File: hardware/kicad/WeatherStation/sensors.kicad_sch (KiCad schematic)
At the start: 16 parts, among them J4 Anemometer (RJ11), J5 Rain Gauge (RJ11), U4 BME280 (0x76), U5 AS5600 (0x36), U6 SI1145 (0x60), U7 BH1750 (0x23)

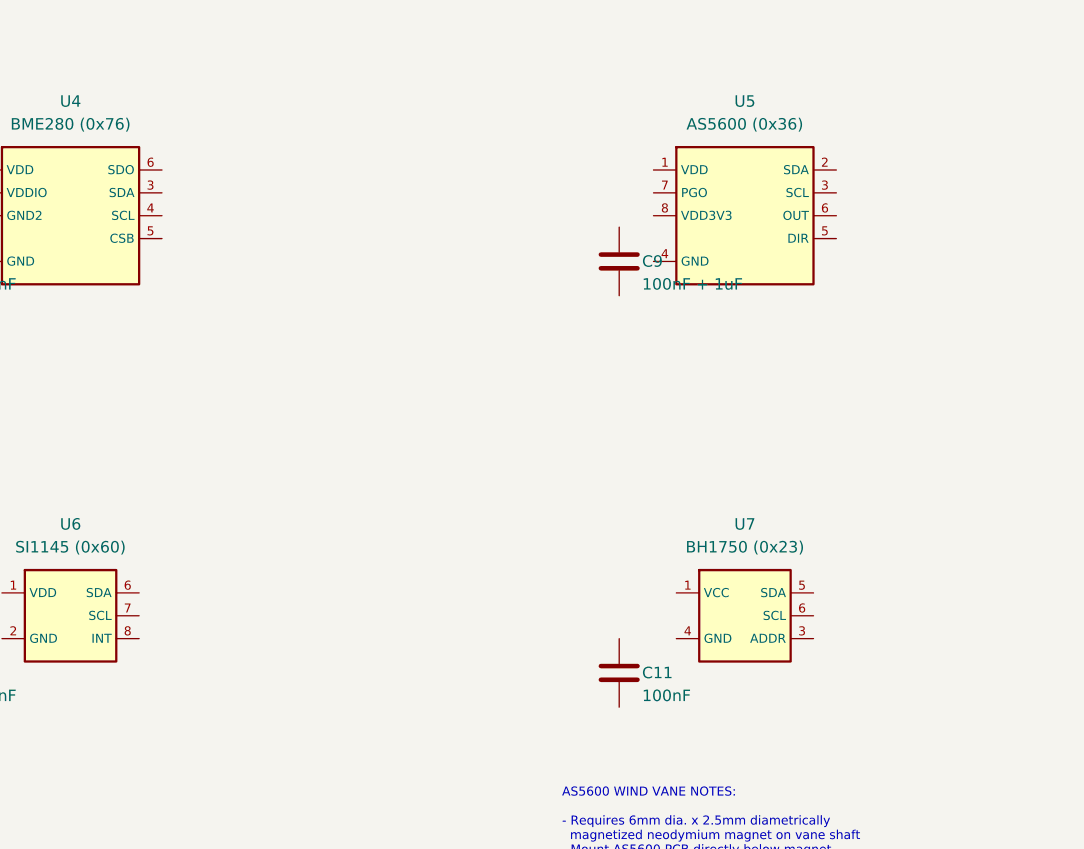
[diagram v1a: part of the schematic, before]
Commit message: Fix 1: sensors.kicad_sch — add BME280 CSB→VCC, SDO→GND; AS5600 DIR→GND, OUT/PGO no-connect; BH1750 ADDR→GND
Agent-Logs-Url: https://github.com/ppusapati/weather/sessions/bf78e071-0670-4802-a032-1f4282b37237

Co-authored-by: ppusapati <5749576+ppusapati@users.noreply.github.com>
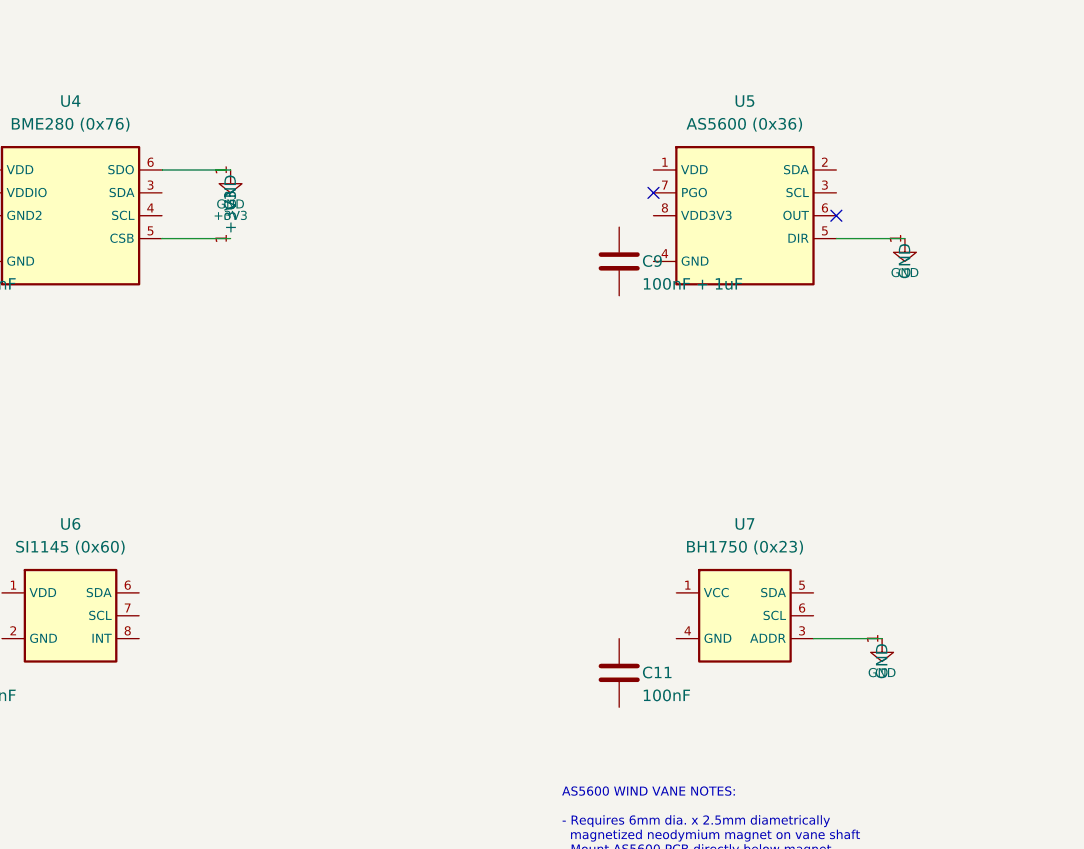
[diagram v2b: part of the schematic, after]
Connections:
- net +3V3: now also U4.5 (CSB)
- net GND: now also U4.6 (SDO), U5.5 (DIR), U7.3 (ADDR)
- no-connect marks 0 -> 2
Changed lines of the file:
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@@
     (at 175.26 130.81 0) (effects (font (size 1.0 1.0)) (justify left))
   )
+  (symbol (lib_id "power:+3V3") (at 138.43 63.50 0) (unit 1)
+    (in_bom yes) (on_board yes) (dnp no)
+    (uuid "fix-bme280-csb-pwr")
+    (property "Reference" "#PWR10" (at 138.43 67.31 0) (effects (font (size 1.0 1.0)) hide))
+    (property "Value" "+3V3" (at 138.43 60.96 0) (effects (font (size 1.0 1.0))))
+    (pin "1" (uuid "fix-bme280-csb-pwr-p1"))
+  )
+  (wire (pts (xy 138.43 63.50) (xy 130.81 63.50))
+    (stroke (width 0) (type default))
+    (uuid "fix-w-bme280-csb")
+  )
+  (symbol (lib_id "power:GND") (at 138.43 55.88 0) (unit 1)
+    (in_bom yes) (on_board yes) (dnp no)
+    (uuid "fix-bme280-sdo-gnd")
+    (property "Reference" "#PWR11" (at 138.43 62.23 0) (effects (font (size 1.0 1.0)) hide))
+    (property "Value" "GND" (at 138.43 59.69 0) (effects (font (size 1.0 1.0))))
+    (pin "1" (uuid "fix-bme280-sdo-gnd-p1"))
+  )
+  (wire (pts (xy 138.43 55.88) (xy 130.81 55.88))
+    (stroke (width 0) (type default))
+    (uuid "fix-w-bme280-sdo")
+  )
+  (symbol (lib_id "power:GND") (at 213.36 63.50 0) (unit 1)
+    (in_bom yes) (on_board yes) (dnp no)
+    (uuid "fix-as5600-dir-gnd")
+    (property "Reference" "#PWR12" (at 213.36 69.85 0) (effects (font (size 1.0 1.0)) hide))
+    (property "Value" "GND" (at 213.36 67.31 0) (effects (font (size 1.0 1.0))))
+    (pin "1" (uuid "fix-as5600-dir-gnd-p1"))
+  )
+  (wire (pts (xy 213.36 63.50) (xy 205.74 63.50))
+    (stroke (width 0) (type default))
+    (uuid "fix-w-as5600-dir")
+  )
+  (no_connect (at 205.74 60.96) (uuid "fix-nc-as5600-out"))
+  (no_connect (at 185.42 58.42) (uuid "fix-nc-as5600-pgo"))
+  (symbol (lib_id "power:GND") (at 210.82 107.95 0) (unit 1)
+    (in_bom yes) (on_board yes) (dnp no)
+    (uuid "fix-bh1750-addr-gnd")
+    (property "Reference" "#PWR13" (at 210.82 114.30 0) (effects (font (size 1.0 1.0)) hide))
+    (property "Value" "GND" (at 210.82 111.76 0) (effects (font (size 1.0 1.0))))
+    (pin "1" (uuid "fix-bh1750-addr-gnd-p1"))
+  )
+  (wire (pts (xy 210.82 107.95) (xy 203.20 107.95))
+    (stroke (width 0) (type default))
+    (uuid "fix-w-bh1750-addr")
+  )
 )
